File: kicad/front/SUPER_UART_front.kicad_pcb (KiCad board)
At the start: 4 copper layers, 100 x 43 mm, 260 parts, among them CON1 PIN-2x4, CON10 PIN-2x5, CON11 PIN-2x12, CON2 PIN-2x3, CON3 RS232, CON4 PORT D, CON5 PORT D, CON6 PORT B, CON7 PORT A, CON8 PORT C, CON9 PIN-2x2, Q1 PDTA143ZT, Q10 2N7002PS, Q11 N-MOS_small, Q12 PDTA143ZT, Q13 N-MOS_small, Q14 N-MOS_small, Q2 PDTA143ZT, Q3 N-MOS_small, Q4 PDTA143ZT, Q5 2N7002PS, Q6 N-MOS_small, Q7 PDTA143ZT, Q8 N-MOS_small, Q9 PDTA143ZT, SW1 5V_1, SW10 3V3_2, SW11 2V5_2, SW12 1V8_2, SW13 I2C_A, SW14 SPI_A, SW15 I2C_B, SW16 SPI_B, SW17 BOOT, SW18 DTR, SW19 RTS, SW2 3V3_1, SW3 2V5_1, SW4 1V8_1, SW5 RX, SW6 TX, SW7 SPY, SW8 ISO, SW9 5V_2, U1 STM32F030R8T6, U10 LP2951CD, U11 74HC595D, U12 74LVC8T245PW, U13 74LVC2T45DCU, U14 74LVC1T45GW, U15 74LVC1T45GW, U16 LP2951CD, U2 MIC5504-3.3YM5-TR, U4 74HC08P, U5 MAX3243EIPW, U6 74HC08P, U7 74LVC8T245PW, U8 74LVC8T245PW, U9 74LVC1T45GW

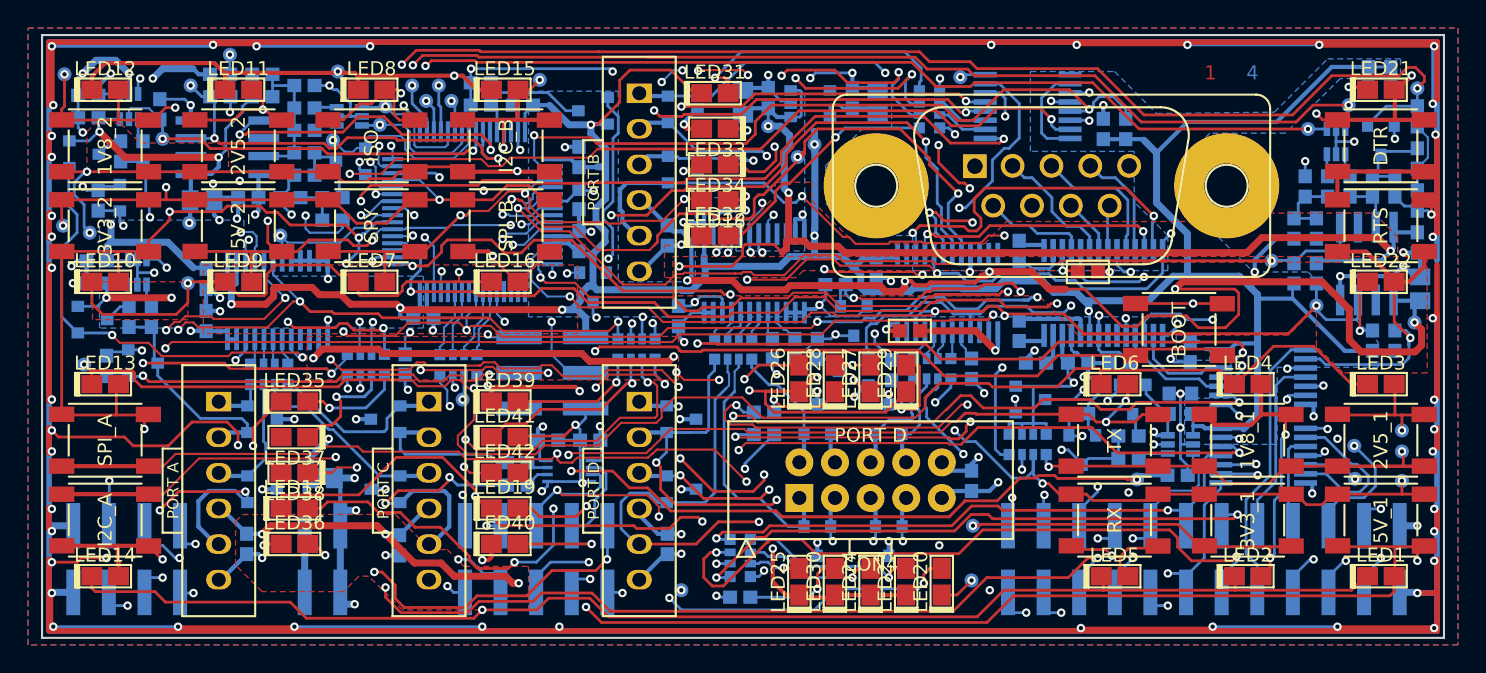
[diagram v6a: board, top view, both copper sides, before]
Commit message: Silkscreen and 3D model updated
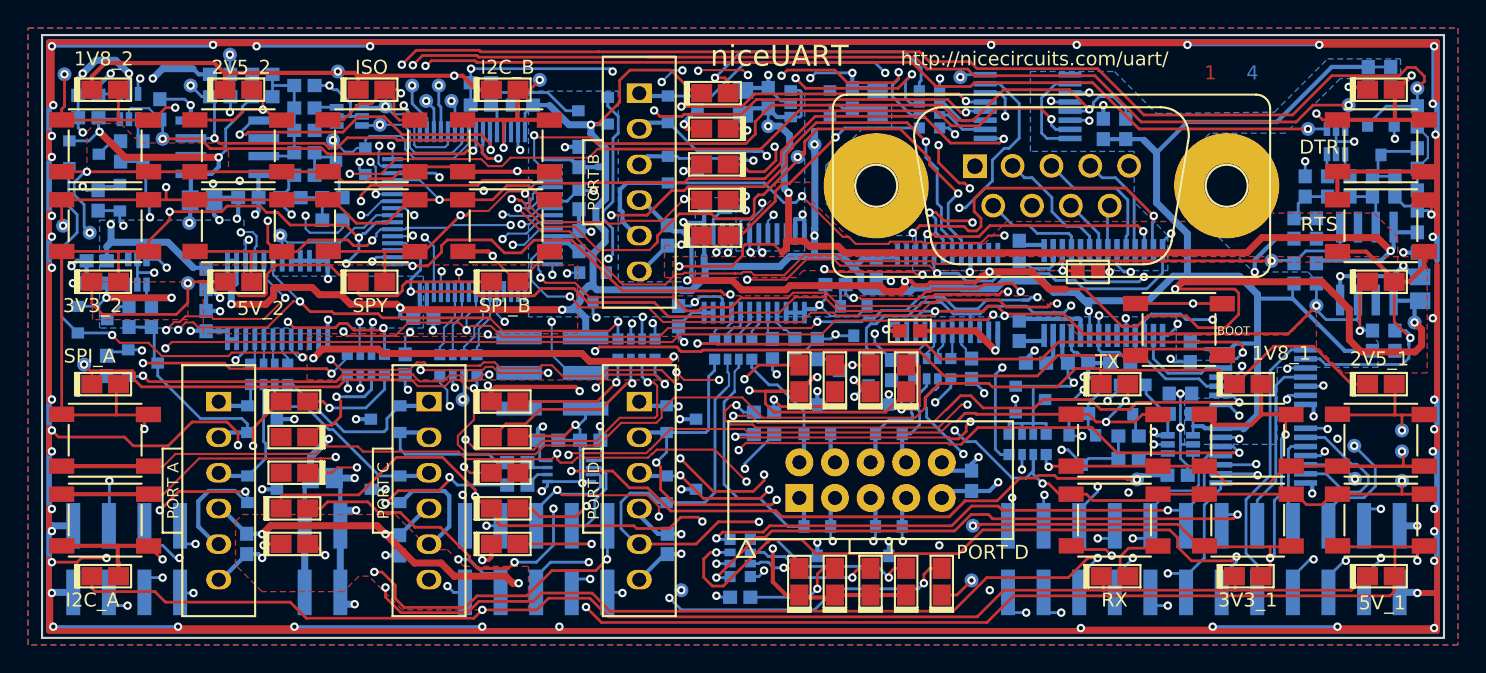
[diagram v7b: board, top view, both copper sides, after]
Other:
- board text added: "NOP040"
- board text added: "http://nicecircuits.com/uart/"
- board text added: "niceUART"

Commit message: Add missing files
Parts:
- added G***: LOGO, pnMechanical:rabbit, B.Cu at (25.8, 47.6)
- Q10, Q5: value 2N7002PS -> N.C.
- Q11, Q6: value N-MOS_small -> N.C.
- R1, R3, R5, RN1: value R -> 220R
- R10, R16, R32, R36: value R -> 4k7
- R11, R12, R17, R30, R31, R33, R39, R9, RN4, RN5, RN7: value R -> 100R
- R13, R14, R7, R8, RN3, RN6, RN8, RN9: value R -> 1k
- R20, R40: value 4k7 -> 100k
- R23, R42: value 1k8 -> 47k
- R24, R43: value 3k9 -> N.C.
- R25, R44: value 6k8 -> N.C.
- R26, R45: value 10k -> 47k
- U11: value 74HC595D -> 74HC595P
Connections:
- net /CLPD_OE renamed /CPLD_OE
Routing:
- net VDD2: track 112.7 -> 107.6 mm
- net GND: track 1294.4 -> 1291.1 mm
- net /~PWREN: track 107.9 -> 108.5 mm
